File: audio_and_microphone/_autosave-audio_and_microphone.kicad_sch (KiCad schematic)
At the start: 30 parts, among them J1 Conn_01x08_MountingPin, J10 Conn_01x02_Pin, J2 Conn_01x03_MountingPin, J3 Conn_01x06_MountingPin, J4 Conn_01x03_Pin, J5 Conn_01x02, J6 Conn_01x10_MountingPin, J7 Conn_01x02, J8 Conn_01x02, J9 Conn_01x02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

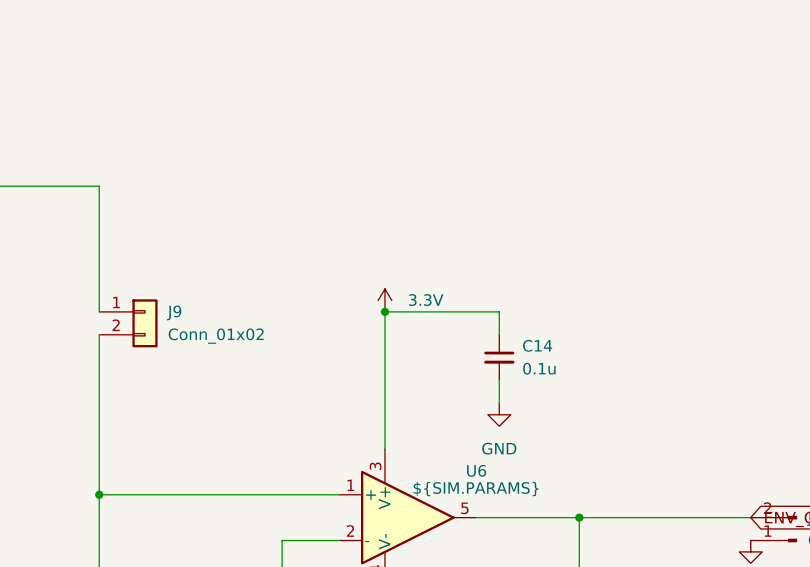
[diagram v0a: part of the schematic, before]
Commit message: changed trace size and 90 degree angles
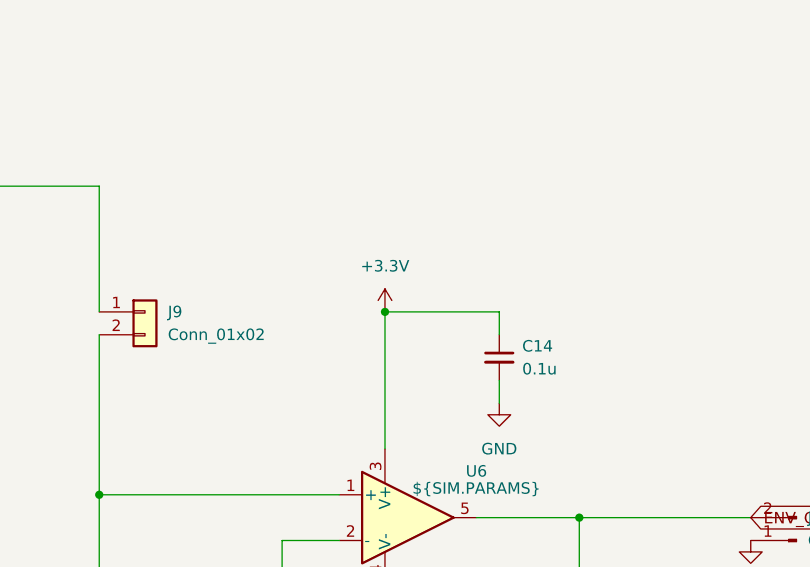
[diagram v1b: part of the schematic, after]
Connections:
- net 3.3V is gone; now on net +3.3V: C14.1, U6.3 (V+)
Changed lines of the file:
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@@
 			)
 		)
-		(property "Value" "3.3V"
-			(at 191.77 81.2799 0)
+		(property "Value" "+3.3V"
+			(at 189.23 77.47 0)
 			(effects
 				(font
 					(size 1.27 1.27)
 				)
-				(justify left)
 			)
 		)

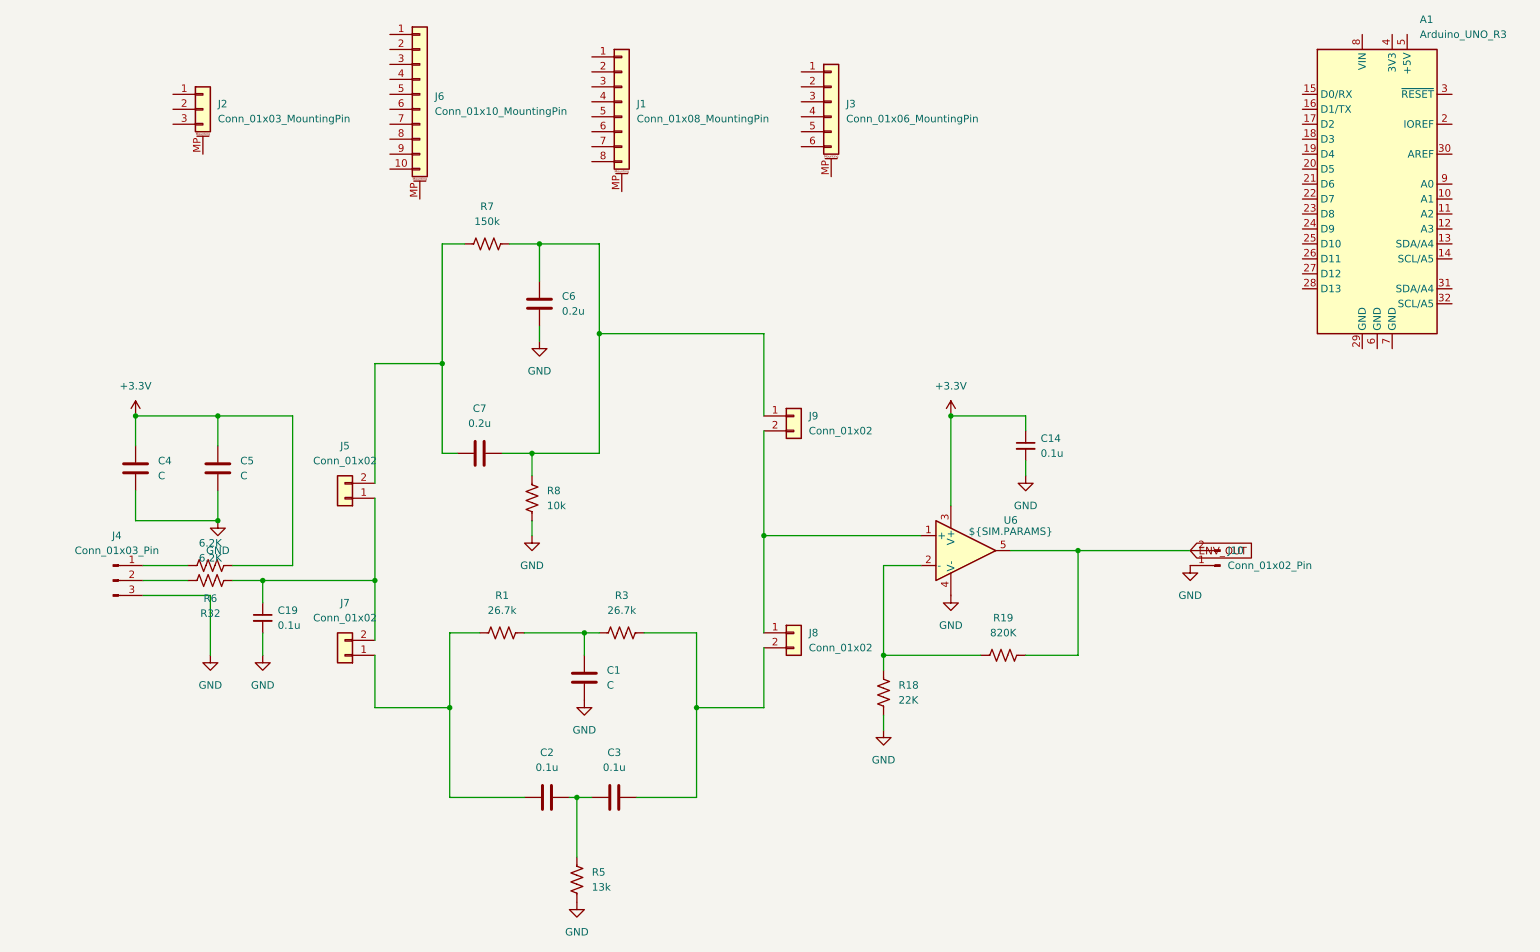
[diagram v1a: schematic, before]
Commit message: updated pcb to be cleaner with net labels and no redundancy
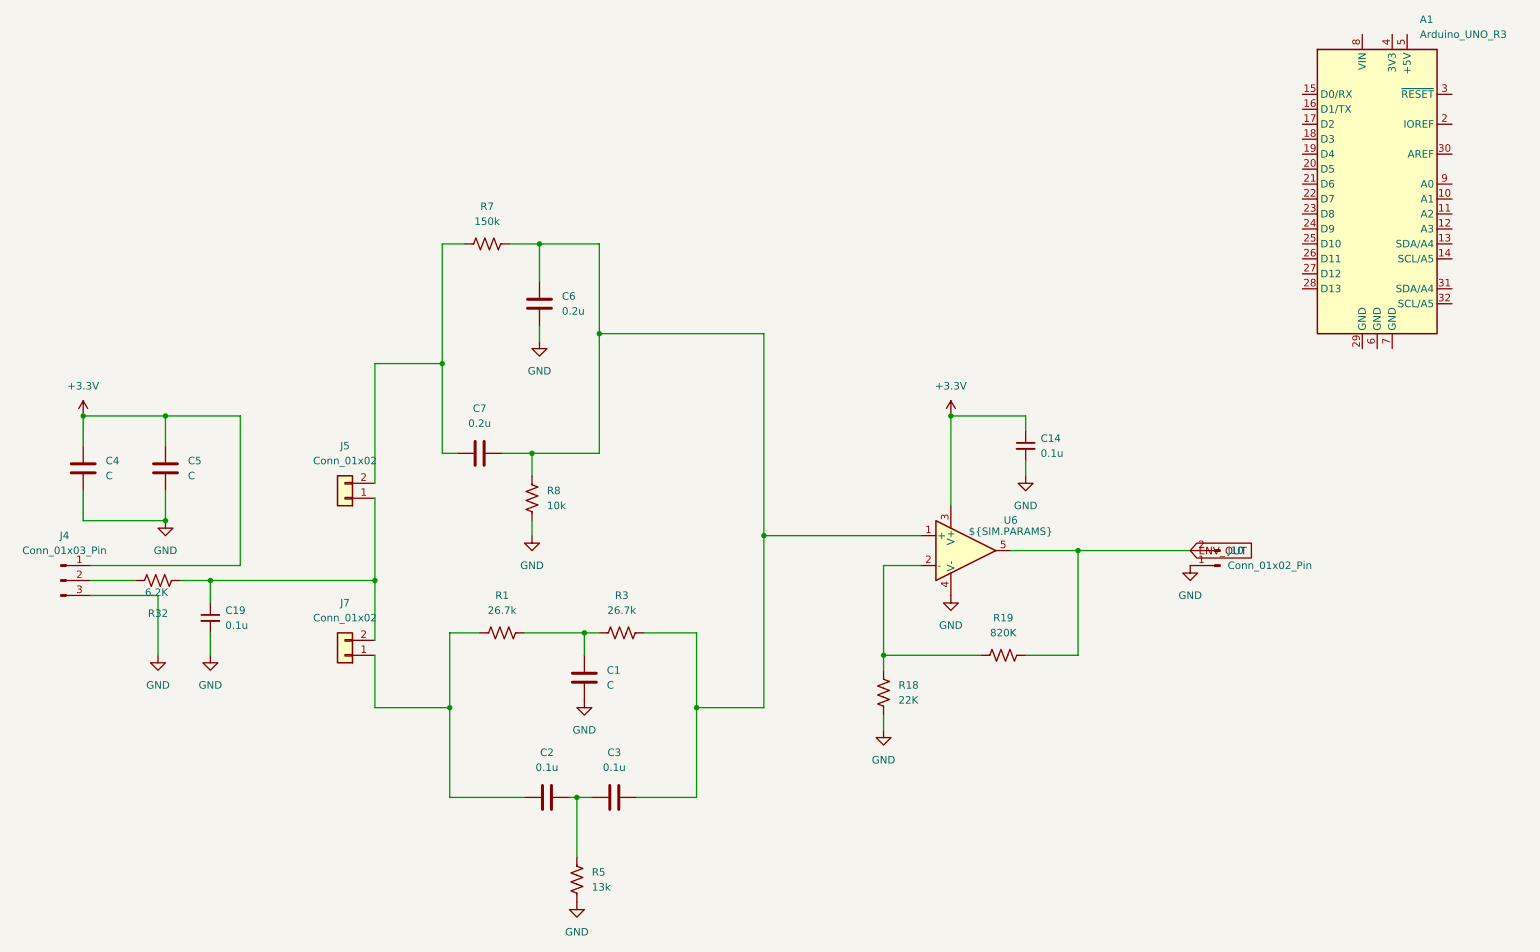
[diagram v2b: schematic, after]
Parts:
- removed J1: Conn_01x08_MountingPin, Connector_PinHeader_2.54mm:PinHeader_1x08_P2.54mm_Vertical, symbol Connector_Generic_MountingPin:Conn_01x08_MountingPin
- removed J2: Conn_01x03_MountingPin, Connector_Harwin:Harwin_M20-89003xx_1x03_P2.54mm_Horizontal, symbol Connector_Generic_MountingPin:Conn_01x03_MountingPin
- removed J3: Conn_01x06_MountingPin, Connector_PinHeader_2.54mm:PinHeader_1x06_P2.54mm_Vertical, symbol Connector_Generic_MountingPin:Conn_01x06_MountingPin
- removed J6: Conn_01x10_MountingPin, Connector_PinHeader_2.54mm:PinHeader_1x10_P2.54mm_Vertical, symbol Connector_Generic_MountingPin:Conn_01x10_MountingPin
- removed J8, J9: Conn_01x02, Connector_PinHeader_2.54mm:PinHeader_1x02_P2.54mm_Vertical, symbol Connector_Generic:Conn_01x02
- removed R6: 6.2K, Resistor_SMD:R_0603_1608Metric_Pad0.98x0.95mm_HandSolder, symbol Device:R_US
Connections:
- net +3.3V: now also J4.1 (Pin_1)
- net at C6.1, C7.2, R7.2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: now also C3.2, R3.2, U6.1 (+)
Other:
- moved on the sheet: C19, C4, C5, J4, R32
